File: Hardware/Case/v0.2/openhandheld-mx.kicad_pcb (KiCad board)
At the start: 2 copper layers, 84 x 89 mm, 0 parts

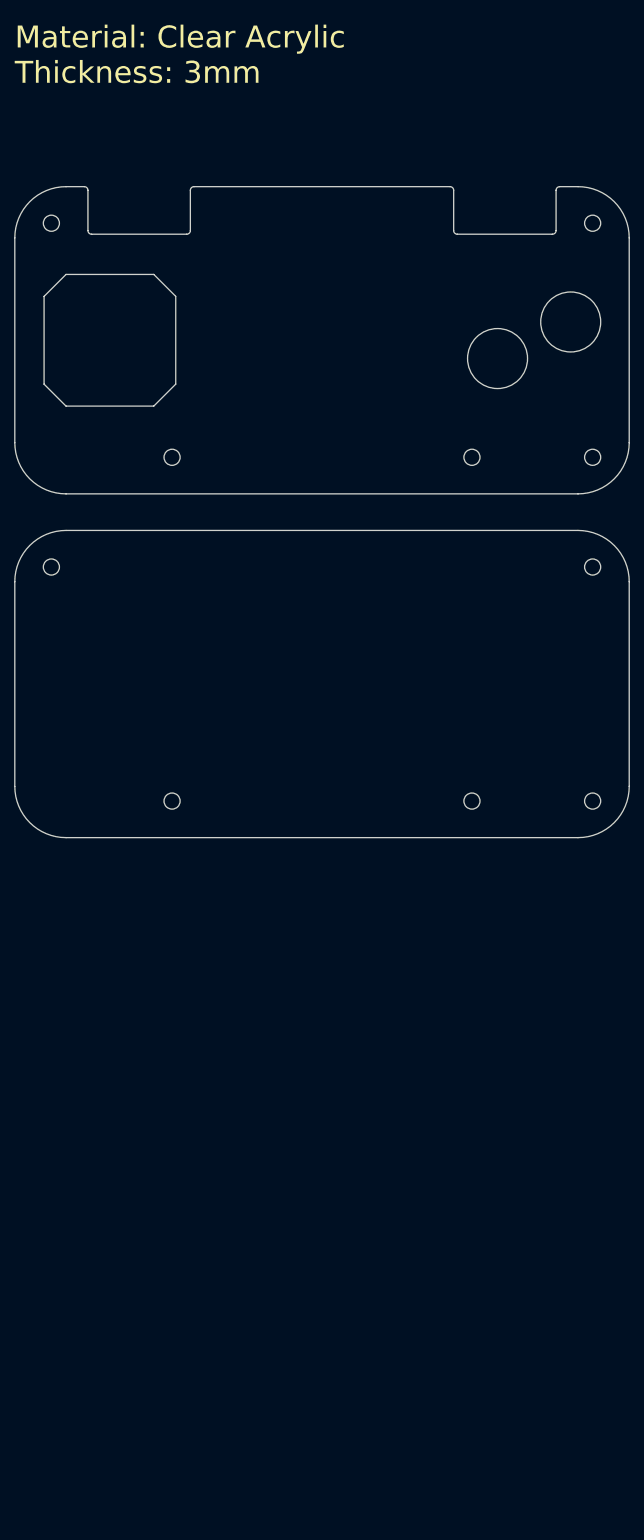
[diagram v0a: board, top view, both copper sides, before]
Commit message: PCB v0.2: Reduced component dimensions. Preliminary placement
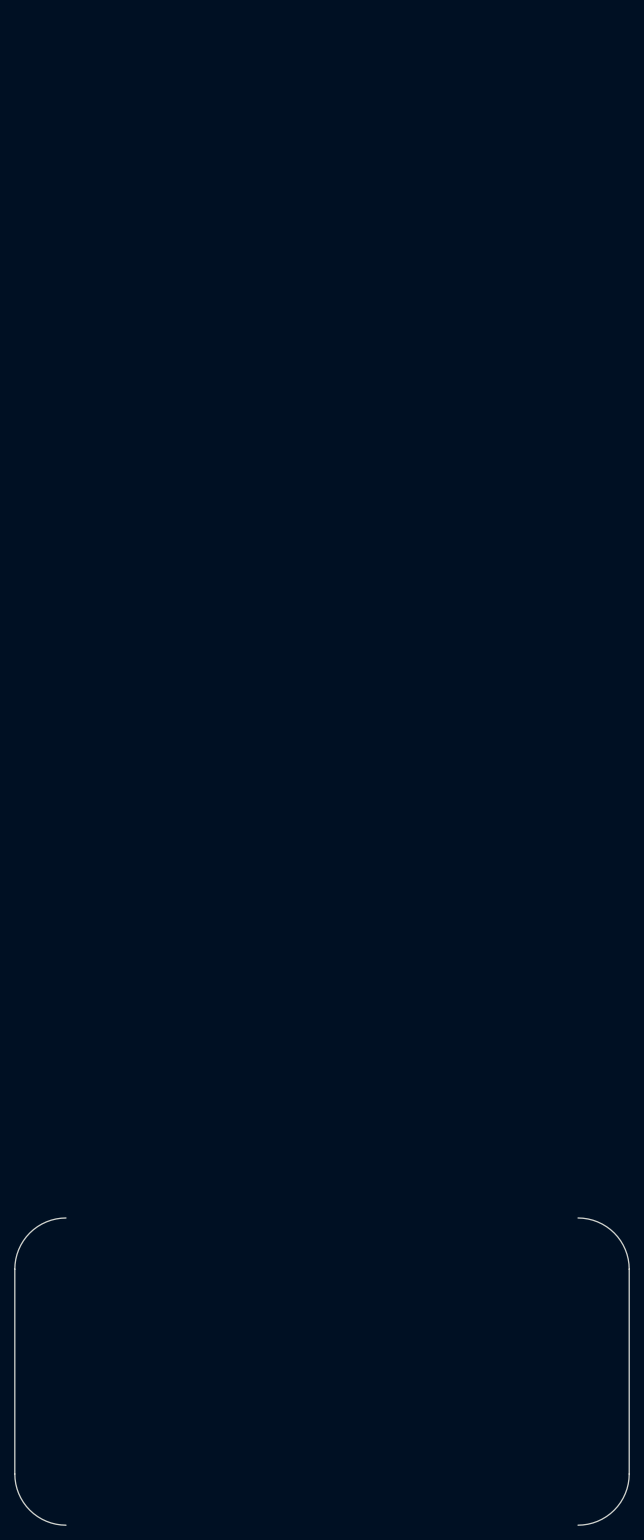
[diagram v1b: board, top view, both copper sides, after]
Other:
- board size 84 x 89 mm -> 84 x 42 mm
- rule pad_to_mask_clearance: 0.051 -> 0
- board text removed: "Material: Clear Acrylic Thickness: 3mm"

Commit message: Case v0.2: Finished
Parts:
- added REF**: ST7789_1.54_240x240, _AKL_Display:ST7789_1.54_240x240, F.Cu at (135.0, 22.5)
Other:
- board size 84 x 42 mm -> 173 x 42 mm
